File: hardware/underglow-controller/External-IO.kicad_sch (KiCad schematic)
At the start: 18 parts, among them Q2 STS8DNF3LL, Q3 STS8DNF3LL, Q5 MBT3904DW1T1G, Q6 MBT3904DW1T1G

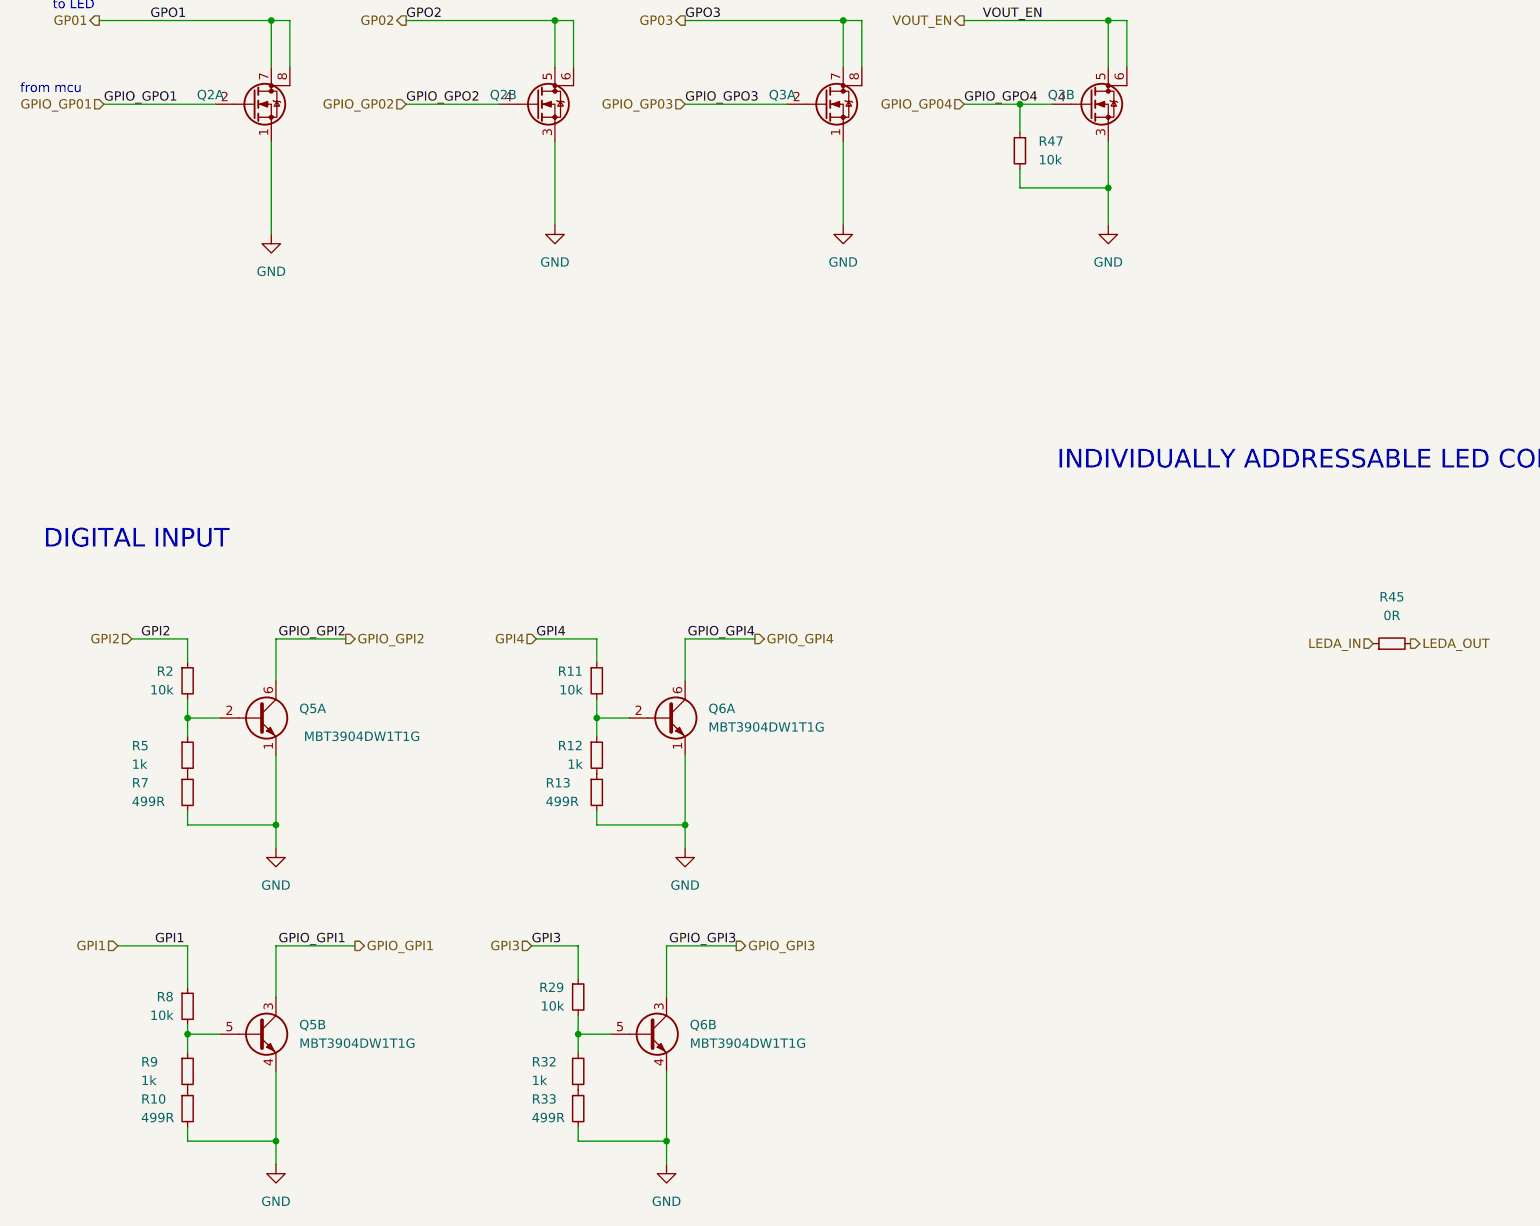
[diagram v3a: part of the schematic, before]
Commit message: add USB VIN
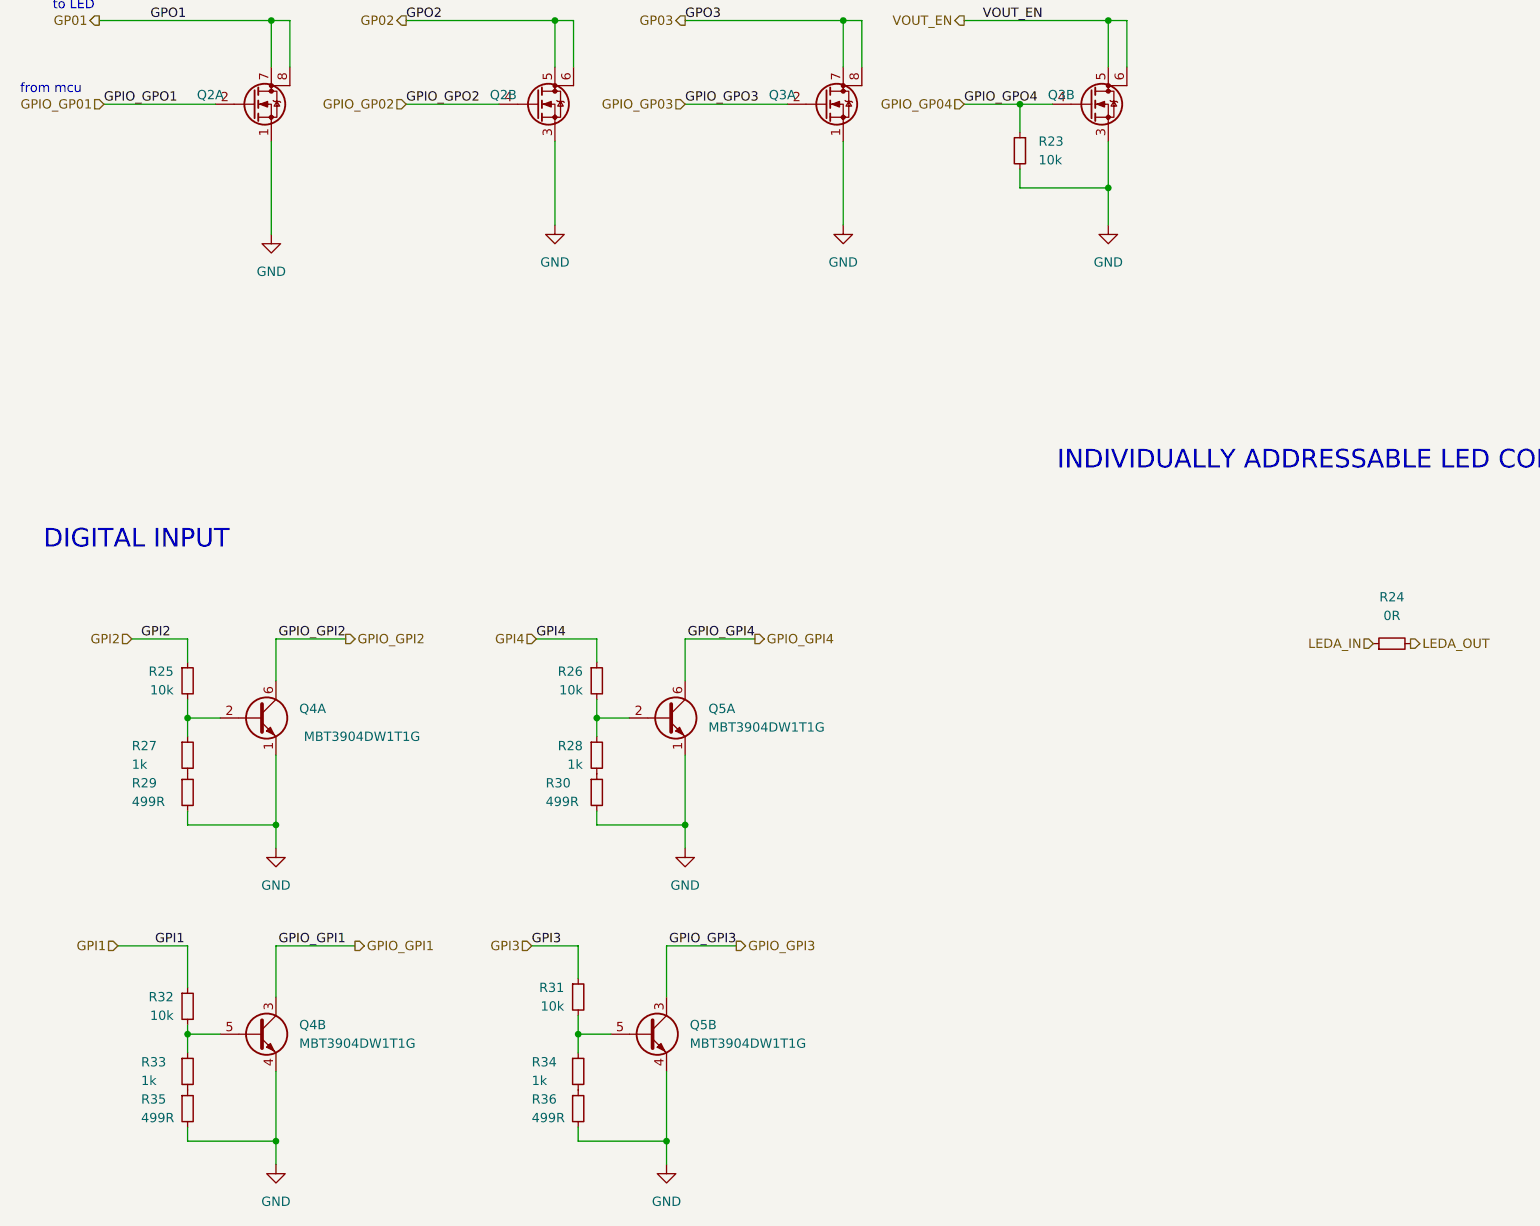
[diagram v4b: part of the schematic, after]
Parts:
- renumbered Q5 to Q4, Q6 to Q5, R47 to R23, R45 to R24, R2 to R25, R11 to R26, R5 to R27, R12 to R28, R7 to R29, R13 to R30, R29 to R31, R8 to R32, R9 to R33, R32 to R34, R10 to R35, R33 to R36
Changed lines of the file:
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@@
   (symbol (lib_id "Device:R_Small") (at 201.93 119.38 90) (unit 1)
     (in_bom yes) (on_board yes) (fields_autoplaced)
-    (property "Reference" "R45" (id 0) (at 201.93 113.03 90))
+    (property "Reference" "R24" (id 0) (at 201.93 113.03 90))
     (property "Value" "0R" (id 1) (at 201.93 115.57 90))
     (property "Footprint" "Resistor_SMD:R_2512_6332Metric" (id 2) (at 201.93 119.38 0)
@@
   (symbol (lib_id "power:GND") (at 49.53 147.32 0) (unit 1)
     (in_bom yes) (on_board yes) (fields_autoplaced)
-    (property "Reference" "#PWR0136" (id 0) (at 49.53 153.67 0)
+    (property "Reference" "#PWR072" (id 0) (at 49.53 153.67 0)
       (effects (font (size 1.27 1.27)) hide)
     )
@@
   (symbol (lib_id "power:GND") (at 48.895 63.5 0) (unit 1)
     (in_bom yes) (on_board yes) (fields_autoplaced)
-    (property "Reference" "#PWR03" (id 0) (at 48.895 69.85 0)
+    (property "Reference" "#PWR071" (id 0) (at 48.895 69.85 0)
       (effects (font (size 1.27 1.27)) hide)
     )
@@
   (symbol (lib_id "Device:Q_Dual_NPN_NPN_E1B1C2E2B2C1") (at 46.99 172.72 0) (unit 2)
     (in_bom yes) (on_board yes) (fields_autoplaced)
-    (property "Reference" "Q5" (id 0) (at 52.705 171.4499 0)
+    (property "Reference" "Q4" (id 0) (at 52.705 171.4499 0)
       (effects (font (size 1.27 1.27)) (justify left))
     )
@@
   (symbol (lib_id "Device:Q_Dual_NPN_NPN_E1B1C2E2B2C1") (at 46.99 129.54 0) (unit 1)
     (in_bom yes) (on_board yes)
-    (property "Reference" "Q5" (id 0) (at 52.705 128.2699 0)
+    (property "Reference" "Q4" (id 0) (at 52.705 128.2699 0)
       (effects (font (size 1.27 1.27)) (justify left))
     )
@@
   (symbol (lib_id "Device:R_Small") (at 37.465 134.62 0) (unit 1)
     (in_bom yes) (on_board yes)
-    (property "Reference" "R5" (id 0) (at 29.845 133.3499 0)
+    (property "Reference" "R27" (id 0) (at 29.845 133.3499 0)
       (effects (font (size 1.27 1.27)) (justify left))
     )
@@
   (symbol (lib_id "Device:R_Small") (at 93.345 139.7 0) (unit 1)
     (in_bom yes) (on_board yes)
-    (property "Reference" "R13" (id 0) (at 86.36 138.4299 0)
+    (property "Reference" "R30" (id 0) (at 86.36 138.4299 0)
       (effects (font (size 1.27 1.27)) (justify left))
     )
@@
   (symbol (lib_id "Device:R_Small") (at 37.465 139.7 0) (unit 1)
     (in_bom yes) (on_board yes)
-    (property "Reference" "R7" (id 0) (at 29.845 138.4299 0)
+    (property "Reference" "R29" (id 0) (at 29.845 138.4299 0)
       (effects (font (size 1.27 1.27)) (justify left))
     )
@@
   (symbol (lib_id "Device:Q_Dual_NPN_NPN_E1B1C2E2B2C1") (at 100.33 172.72 0) (unit 2)
     (in_bom yes) (on_board yes) (fields_autoplaced)
-    (property "Reference" "Q6" (id 0) (at 106.045 171.4499 0)
+    (property "Reference" "Q5" (id 0) (at 106.045 171.4499 0)
       (effects (font (size 1.27 1.27)) (justify left))
     )
@@
   (symbol (lib_id "power:GND") (at 105.41 147.32 0) (unit 1)
     (in_bom yes) (on_board yes) (fields_autoplaced)
-    (property "Reference" "#PWR0148" (id 0) (at 105.41 153.67 0)
+    (property "Reference" "#PWR073" (id 0) (at 105.41 153.67 0)
       (effects (font (size 1.27 1.27)) hide)
     )
@@
   (symbol (lib_id "Device:R_Small") (at 90.805 167.64 0) (unit 1)
     (in_bom yes) (on_board yes) (fields_autoplaced)
-    (property "Reference" "R29" (id 0) (at 88.9 166.3699 0)
+    (property "Reference" "R31" (id 0) (at 88.9 166.3699 0)
       (effects (font (size 1.27 1.27)) (justify right))
     )
@@
   (symbol (lib_id "Device:Q_Dual_NPN_NPN_E1B1C2E2B2C1") (at 102.87 129.54 0) (unit 1)
     (in_bom yes) (on_board yes) (fields_autoplaced)
-    (property "Reference" "Q6" (id 0) (at 108.585 128.2699 0)
+    (property "Reference" "Q5" (id 0) (at 108.585 128.2699 0)
       (effects (font (size 1.27 1.27)) (justify left))
     )
@@
   (symbol (lib_id "power:GND") (at 102.87 190.5 0) (unit 1)
     (in_bom yes) (on_board yes) (fields_autoplaced)
-    (property "Reference" "#PWR0157" (id 0) (at 102.87 196.85 0)
+    (property "Reference" "#PWR075" (id 0) (at 102.87 196.85 0)
       (effects (font (size 1.27 1.27)) hide)
     )
@@
   (symbol (lib_id "Device:R_Small") (at 90.805 182.88 0) (unit 1)
     (in_bom yes) (on_board yes)
-    (property "Reference" "R33" (id 0) (at 84.455 181.6099 0)
+    (property "Reference" "R36" (id 0) (at 84.455 181.6099 0)
       (effects (font (size 1.27 1.27)) (justify left))
     )
@@
   (symbol (lib_id "Device:R_Small") (at 37.465 182.88 0) (unit 1)
     (in_bom yes) (on_board yes)
-    (property "Reference" "R10" (id 0) (at 31.115 181.6099 0)
+    (property "Reference" "R35" (id 0) (at 31.115 181.6099 0)
       (effects (font (size 1.27 1.27)) (justify left))
     )
@@
   (symbol (lib_id "Device:R_Small") (at 37.465 168.91 0) (unit 1)
     (in_bom yes) (on_board yes) (fields_autoplaced)
-    (property "Reference" "R8" (id 0) (at 35.56 167.6399 0)
+    (property "Reference" "R32" (id 0) (at 35.56 167.6399 0)
       (effects (font (size 1.27 1.27)) (justify right))
     )
@@
   (symbol (lib_id "power:GND") (at 127 62.23 0) (unit 1)
     (in_bom yes) (on_board yes) (fields_autoplaced)
-    (property "Reference" "#PWR06" (id 0) (at 127 68.58 0)
+    (property "Reference" "#PWR069" (id 0) (at 127 68.58 0)
       (effects (font (size 1.27 1.27)) hide)
     )
@@
   (symbol (lib_id "power:GND") (at 49.53 190.5 0) (unit 1)
     (in_bom yes) (on_board yes) (fields_autoplaced)
-    (property "Reference" "#PWR0137" (id 0) (at 49.53 196.85 0)
+    (property "Reference" "#PWR074" (id 0) (at 49.53 196.85 0)
       (effects (font (size 1.27 1.27)) hide)
     )
@@
   (symbol (lib_id "Device:R_Small") (at 37.465 124.46 0) (unit 1)
     (in_bom yes) (on_board yes) (fields_autoplaced)
-    (property "Reference" "R2" (id 0) (at 35.56 123.1899 0)
+    (property "Reference" "R25" (id 0) (at 35.56 123.1899 0)
       (effects (font (size 1.27 1.27)) (justify right))
     )
@@
   (symbol (lib_id "Device:R_Small") (at 93.345 124.46 0) (unit 1)
     (in_bom yes) (on_board yes) (fields_autoplaced)
-    (property "Reference" "R11" (id 0) (at 91.44 123.1899 0)
+    (property "Reference" "R26" (id 0) (at 91.44 123.1899 0)
       (effects (font (size 1.27 1.27)) (justify right))
     )
@@
   (symbol (lib_id "Device:R_Small") (at 90.805 177.8 0) (unit 1)
     (in_bom yes) (on_board yes)
-    (property "Reference" "R32" (id 0) (at 84.455 176.5299 0)
+    (property "Reference" "R34" (id 0) (at 84.455 176.5299 0)
       (effects (font (size 1.27 1.27)) (justify left))
     )
@@
   (symbol (lib_id "power:GND") (at 87.63 62.23 0) (unit 1)
     (in_bom yes) (on_board yes) (fields_autoplaced)
-    (property "Reference" "#PWR02" (id 0) (at 87.63 68.58 0)
+    (property "Reference" "#PWR068" (id 0) (at 87.63 68.58 0)
       (effects (font (size 1.27 1.27)) hide)
     )
@@
   (symbol (lib_id "Device:R_Small") (at 37.465 177.8 0) (unit 1)
     (in_bom yes) (on_board yes)
-    (property "Reference" "R9" (id 0) (at 31.115 176.5299 0)
+    (property "Reference" "R33" (id 0) (at 31.115 176.5299 0)
       (effects (font (size 1.27 1.27)) (justify left))
     )
@@
   (symbol (lib_id "Device:R_Small") (at 151.13 52.07 0) (mirror y) (unit 1)
     (in_bom yes) (on_board yes) (fields_autoplaced)
-    (property "Reference" "R47" (id 0) (at 153.67 50.7999 0)
+    (property "Reference" "R23" (id 0) (at 153.67 50.7999 0)
       (effects (font (size 1.27 1.27)) (justify right))
     )
@@
   (symbol (lib_id "Device:R_Small") (at 93.345 134.62 0) (unit 1)
     (in_bom yes) (on_board yes) (fields_autoplaced)
-    (property "Reference" "R12" (id 0) (at 91.44 133.3499 0)
+    (property "Reference" "R28" (id 0) (at 91.44 133.3499 0)
       (effects (font (size 1.27 1.27)) (justify right))
     )
@@
   (symbol (lib_id "power:GND") (at 163.195 62.23 0) (unit 1)
     (in_bom yes) (on_board yes) (fields_autoplaced)
-    (property "Reference" "#PWR09" (id 0) (at 163.195 68.58 0)
-      (effects (font (size 1.27 1.27)) hide)
-    )
+    (property "Reference" "#PWR070" (id 0) (at 163.195 68.58 0)
+      (effects (font (size 1.27 1.27)) hide)
+    )

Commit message: Hardware updates
* fix messed up +12v pin
* add a ground output for neopixels on both channels
* add a i2c microphone
* clean up schematic
* calculate component values for the LED drivers
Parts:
- removed R23: 10k, Resistor_SMD:R_0603_1608Metric, symbol Device:R_Small
- added ALED601, ALED602: WS2815B, worldsemi-WS2815B-*, symbol ConeCodes:WS2815B
- added C601, C606: 47uF, Capacitor_SMD:CP_Elec_6.3x7.7, symbol Device:C_Polarized_Small
- added C602, C607: 4.7uF X5R, Capacitor_SMD:C_1206_3216Metric, symbol Device:C_Small
- added C603, C604, C608, C609: 0.1uF, Capacitor_SMD:C_0603_1608Metric, symbol Device:C_Small
- added C605, C610: 0.68μF,DNF, Capacitor_SMD:C_1206_3216Metric, symbol Device:C
- added D601, D602: B250A-13-F, ConeCodes:DIOM5226X240N, symbol Device:D_Schottky_Small
- added L601, L602: 74438356033, Inductor_SMD:L_Wuerth_MAPI-4030, symbol Device:L_Small
- added Q603: STS8DNF3LL, Package_SO:SO-8_3.9x4.9mm_P1.27mm, symbol Device:Q_Dual_NMOS_S1G1S2G2D2D2D1D1
- added R24: 0R, Resistor_SMD:R_2512_6332Metric, symbol Device:R_Small
- added R601, R604: 66.9, Resistor_SMD:R_0603_1608Metric, symbol Device:R_Small
- added R602, R605: 0R067, Resistor_SMD:R_1206_3216Metric, symbol Device:R_Small
- added R603, R606: 10k, Resistor_SMD:R_0603_1608Metric, symbol Device:R_Small
- added U601, U602: A6213-1, Package_SO:SOIC-8-1EP_3.9x4.9mm_P1.27mm_EP2.41x3.3mm_ThermalVias, symbol ConeCodes:A6213-1
- renumbered Q2 to Q601, Q3 to Q602, Q4 to Q604, Q5 to Q605, R24 to R23, R25 to R607, R27 to R608, R29 to R609, R26 to R610, R28 to R611, R30 to R612, R32 to R613, R33 to R614, R35 to R615, R31 to R616, R34 to R617, R36 to R618
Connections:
- net GND: now also C601.2, C602.1, C604.2, C606.2, C607.1, C609.2, D601.2 (A), D602.2 (A), R602.2, R603.1, R605.2, R606.1, U601.6 (GND), U601.9 (EP), U602.6 (GND), U602.9 (EP); no longer Q601.1 (S), Q601.3 (S), Q602.1 (S), Q602.3 (S)
- net GP01 renamed RGB1_R
- net GP02 renamed RGB1_G
- net GP03 renamed RGB1_B
- net GPI1 renamed DI_1
- net GPI2 renamed DI_2
- net GPI3 renamed DI_3
- net GPI4 renamed DI_4
- net GPIO_GP01 renamed TTL_RGB1_R
- net GPIO_GP02 renamed TTL_RGB1_G
- net GPIO_GP03 renamed TTL_RGB1_B
- net GPIO_GP04 renamed TTL_RGB2_R
- net GPIO_GPI1 renamed TTL_DI_1
- net GPIO_GPI2 renamed TTL_DI_2
- net GPIO_GPI3 renamed TTL_DI_3
- net GPIO_GPI4 renamed TTL_DI_4
- net LEDA_IN renamed PIXEL1_IN
- net PIXEL1_IN: now also ALED601.4 (DIN)
- net LEDA_OUT renamed PIXEL1_OUT
- net PIXEL1_OUT: now also ALED601.3 (DO)
- net VOUT_EN renamed RGB2_R
- new net: R604.2, U602.2 (TON)
- new net: R601.2, U601.2 (TON)
- new net PIXEL2_IN: ALED602.4 (DIN), R24.1
- new net PIXEL2_OUT: ALED602.3 (DO), R24.2
- new net PWMI1: R603.2, U601.3 (EN)
- new net PWMI2: R606.2, U602.3 (EN)
- new net RGB1_12V: ALED601.2 (VDD), C605.1, L601.2
- new net RGB1_BOOT: C603.1, U601.7 (BOOT)
- new net RGB1_GND: ALED601.5 (GND), C605.2, Q601.1 (S), Q601.3 (S), Q602.1 (S), R602.1, U601.4 (CS)
- new net RGB1_SW: C603.2, D601.1 (K), L601.1, U601.8 (SW)
- new net RGB1_VCC: C604.1, U601.5 (VCC)
- new net RGB2_12V: ALED602.2 (VDD), C610.1, L602.2
- new net RGB2_B: Q603.5 (D), Q603.6 (D)
- new net RGB2_BOOT: C608.1, U602.7 (BOOT)
- new net RGB2_G: Q603.7 (D), Q603.8 (D)
- new net RGB2_GND: ALED602.5 (GND), C610.2, Q602.3 (S), Q603.1 (S), Q603.3 (S), R605.1, U602.4 (CS)
- new net RGB2_SW: C608.2, D602.1 (K), L602.1, U602.8 (SW)
- new net RGB2_VCC: C609.1, U602.5 (VCC)
- new net TTL_RGB2_B: Q603.4 (G)
- new net TTL_RGB2_G: Q603.2 (G)
- new net VBATT: C601.1, C602.2, C606.1, C607.2, R601.1, R604.1, U601.1 (VIN), U602.1 (VIN)
- no-connect marks 0 -> 4
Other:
- note added: "Channel #1"
- note added: "Channel #1 N-Channel Fet arrays"
- note added: "Channel #1 Voltage Regulator"
- note added: "Channel #2"
- note added: "Channel #2 N-Channel Fet arrays"
- note added: "Channel #2 Voltage Regulator"
- note added: "Current Sense Anything powered by this channel should be grounded thru this resistor"
- note added: "N-Channel low side Mosfets driven at TTL levels, drivers might be necessary"
- note added: "The A6213 is designed to operate without an output filter capaci- tor, in order to save cost. Adding a large output capacitor is not recommended"
- note added: "WS2815B Control These two LEDs are not actually fitted on the board, they are here to show how the LEDs are connected externally at the connector"
- title: CAN RGB Controller -> CAN RGB Controller V5
- moved on the sheet: Q601A, Q601B, Q602A, Q602B, Q604A, Q604B, Q605A, Q605B, R23, R607, R608, R609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
